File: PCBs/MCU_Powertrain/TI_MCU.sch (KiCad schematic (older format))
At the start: 1 part

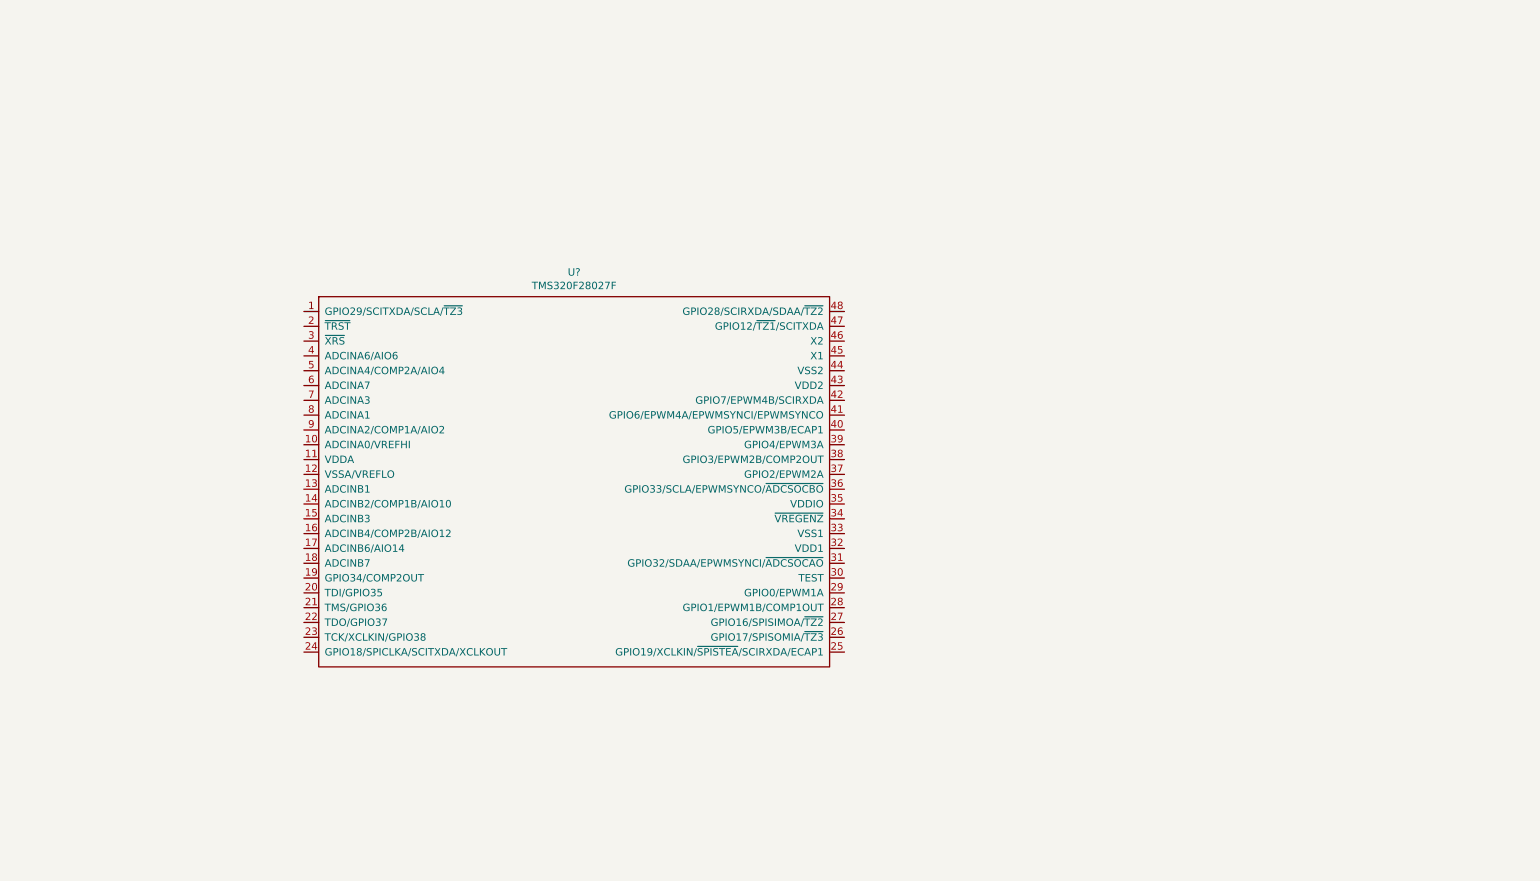
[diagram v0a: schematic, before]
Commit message: Updated TI_MCU Sheet
-Added all required components onto the TI-MCU sheet other than the external connections (header pins on the dev board)
- Added pulldown and pullup resistors for proper JTAG debug and flashing functionality.
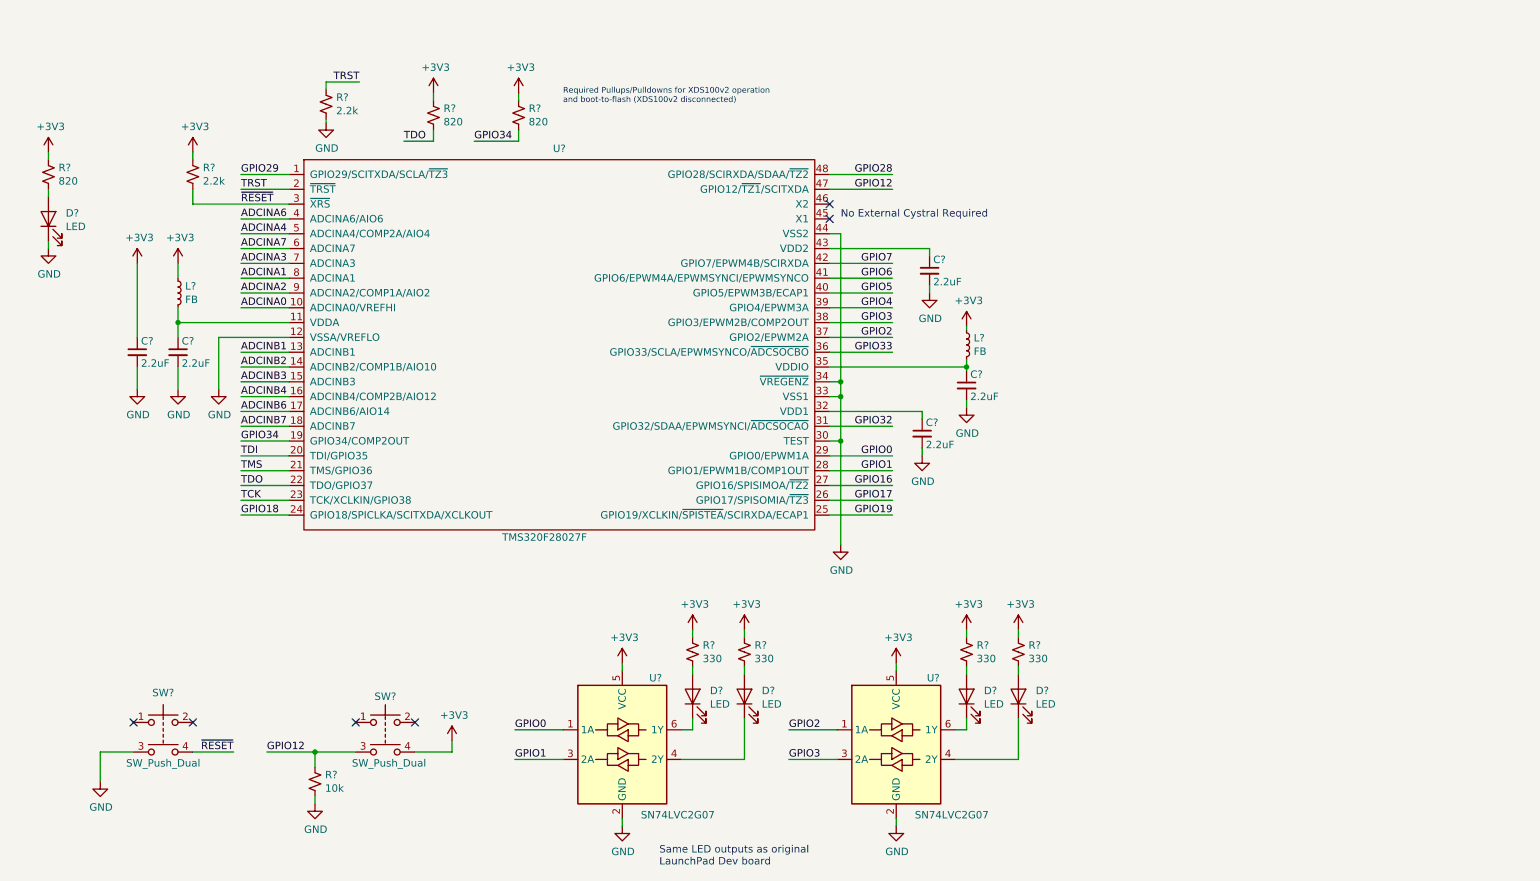
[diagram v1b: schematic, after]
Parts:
- added C? (x5): 2.2uF, symbol Device:C_Small
- added D? (x5): LED, symbol Device:LED
- added L? (x2): FB, symbol Device:L_Small
- added R? (x3): 820, symbol Device:R_Small_US
- added R? (x2): 2.2k, symbol Device:R_Small_US
- added R? (x4): 330, symbol Device:R_Small_US
- added R?: 10k, symbol Device:R_Small_US
- added SW? (x2): SW_Push_Dual, symbol Switch:SW_Push_Dual
- added U? (x2): SN74LVC2G07, Package_SO:VSSOP-8_2.4x2.1mm_P0.5mm, symbol MCU_Powertrain:SN74LVC2G07
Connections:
- net GPIO29: now reaches U?.1 (GPIO29/SCITXDA/SCLA/~TZ3~)
- net ADCINA0: now reaches U?.10 (ADCINA0/VREFHI)
- net at U?.11 (VDDA): now also C?.1, L?.2
- net GND: now reaches U?.12 (VSSA/VREFLO)
- net GND: now also U?.30 (TEST), U?.33 (VSS1), U?.34 (~VREGENZ~), U?.44 (VSS2), C?.2, C?.2, C?.2, C?.2, C?.2, D?.1 (K), R?.2, R?.2, SW?.3, U?.2 (GND), U?.2 (GND)
- net ADCINB1: now reaches U?.13 (ADCINB1)
- net ADCINB2: now reaches U?.14 (ADCINB2/COMP1B/AIO10)
- net ADCINB3: now reaches U?.15 (ADCINB3)
- net ADCINB4: now reaches U?.16 (ADCINB4/COMP2B/AIO12)
- net ADCINB6: now reaches U?.17 (ADCINB6/AIO14)
- net ADCINB7: now reaches U?.18 (ADCINB7)
- net GPIO34: now reaches U?.19 (GPIO34/COMP2OUT)
- net GPIO34: now also R?.2
- net TRST: now reaches U?.2 (~TRST~)
- net TRST: now also R?.1
- net TDI: now reaches U?.20 (TDI/GPIO35)
- net TMS: now reaches U?.21 (TMS/GPIO36)
- net TDO: now reaches U?.22 (TDO/GPIO37)
- net TDO: now also R?.2
- net TCK: now reaches U?.23 (TCK/XCLKIN/GPIO38)
- net GPIO18: now reaches U?.24 (GPIO18/SPICLKA/SCITXDA/XCLKOUT)
- net GPIO19: now reaches U?.25 (GPIO19/XCLKIN/~SPISTEA~/SCIRXDA/ECAP1)
- net GPIO17: now reaches U?.26 (GPIO17/SPISOMIA/~TZ3)
- net GPIO16: now reaches U?.27 (GPIO16/SPISIMOA/~TZ2~)
- net GPIO1: now reaches U?.28 (GPIO1/EPWM1B/COMP1OUT)
- net GPIO1: now also U?.3 (2A)
- net GPIO0: now reaches U?.29 (GPIO0/EPWM1A)
- net GPIO0: now also U?.1 (1A)
- net ~RESET~: now reaches U?.3 (~XRS~)
- net ~RESET~: now also R?.2, SW?.4
- net GPIO32: now reaches U?.31 (GPIO32/SDAA/EPWMSYNCI/~ADCSOCAO~)
- net at U?.32 (VDD1): now also C?.1
- net at U?.35 (VDDIO): now also C?.1, L?.2
- net GPIO33: now reaches U?.36 (GPIO33/SCLA/EPWMSYNCO/~ADCSOCBO~)
- net GPIO2: now reaches U?.37 (GPIO2/EPWM2A)
- net GPIO2: now also U?.1 (1A)
- net GPIO3: now reaches U?.38 (GPIO3/EPWM2B/COMP2OUT)
- net GPIO3: now also U?.3 (2A)
- net GPIO4: now reaches U?.39 (GPIO4/EPWM3A)
- net ADCINA6: now reaches U?.4 (ADCINA6/AIO6)
- net GPIO5: now reaches U?.40 (GPIO5/EPWM3B/ECAP1)
- net GPIO6: now reaches U?.41 (GPIO6/EPWM4A/EPWMSYNCI/EPWMSYNCO)
- net GPIO7: now reaches U?.42 (GPIO7/EPWM4B/SCIRXDA)
- net at U?.43 (VDD2): now also C?.1
- net GPIO12: now reaches U?.47 (GPIO12/~TZ1~/SCITXDA)
- net GPIO12: now also R?.1, SW?.3
- net GPIO28: now reaches U?.48 (GPIO28/SCIRXDA/SDAA/~TZ2~)
- net ADCINA4: now reaches U?.5 (ADCINA4/COMP2A/AIO4)
- net ADCINA7: now reaches U?.6 (ADCINA7)
- net ADCINA3: now reaches U?.7 (ADCINA3)
- net ADCINA1: now reaches U?.8 (ADCINA1)
- net ADCINA2: now reaches U?.9 (ADCINA2/COMP1A/AIO2)
- new net: D?.2 (A), R?.2 (x5)
- new net: D?.1 (K), U?.4 (2Y) (x2)
- new net: D?.1 (K), U?.6 (1Y) (x2)
- new net +3V3: C?.1, L?.1, L?.1, R?.1, R?.1, R?.1, R?.1, R?.1, R?.1, R?.1, R?.1, SW?.4, U?.5 (VCC), U?.5 (VCC)
- no-connect marks 0 -> 6
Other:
- note added: "No External Cystral Required"
- note added: "Required Pullups/Pulldowns for XDS100v2 operation \nand boot-to-flash (XDS100v2 disconnected)"
- note added: "Same LED outputs as original\nLaunchPad Dev board"
- moved on the sheet: U?

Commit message: More Schematic Changes
- Connected TI_MCU schematic to Powertrain schematic
- Added power input
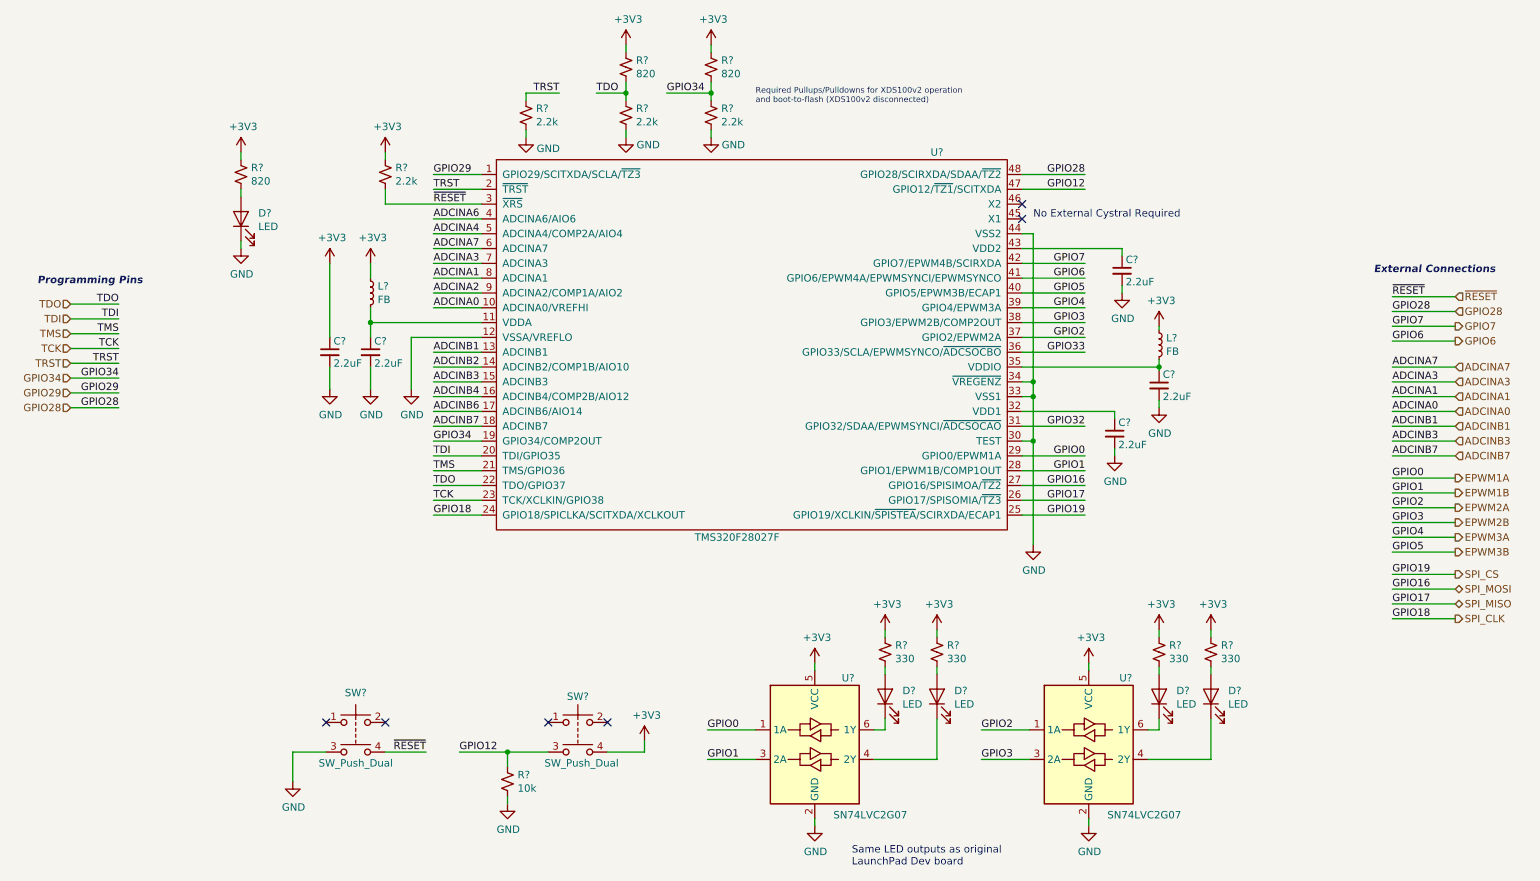
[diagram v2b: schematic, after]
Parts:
- added R? (x2): 2.2k, symbol Device:R_Small_US
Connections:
- net GND: now also R?.2, R?.2
- net GPIO34: now also R?.1
- net TDO: now also R?.1
- net GPIO0 renamed EPWM1A
- net GPIO1 renamed EPWM1B
- net GPIO16 renamed SPI_MOSI
- net GPIO17 renamed SPI_MISO
- net GPIO18 renamed SPI_CLK
- net GPIO19 renamed SPI_CS
- net GPIO2 renamed EPWM2A
- net GPIO3 renamed EPWM2B
- net GPIO4 renamed EPWM3A
- net GPIO5 renamed EPWM3B
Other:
- note added: "External Connections"
- note added: "Programming Pins"
- moved on the sheet: C?, D?, L?, R?, SW?, U?

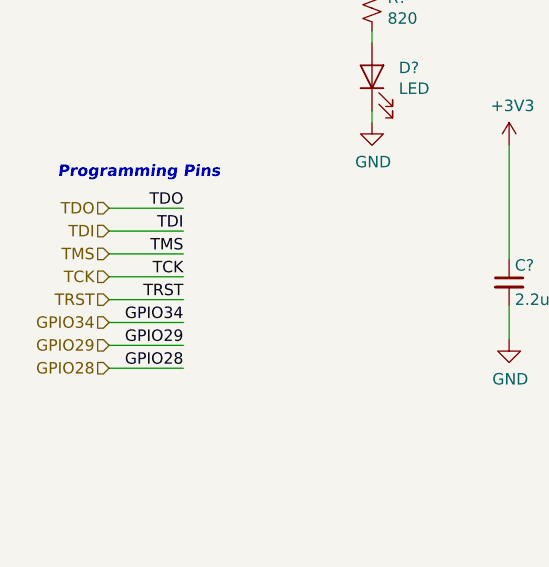
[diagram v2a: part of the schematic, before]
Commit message: Added Programming Headers
- Inserted programming headers based on latest header format from custom XDS100v2 programmer.
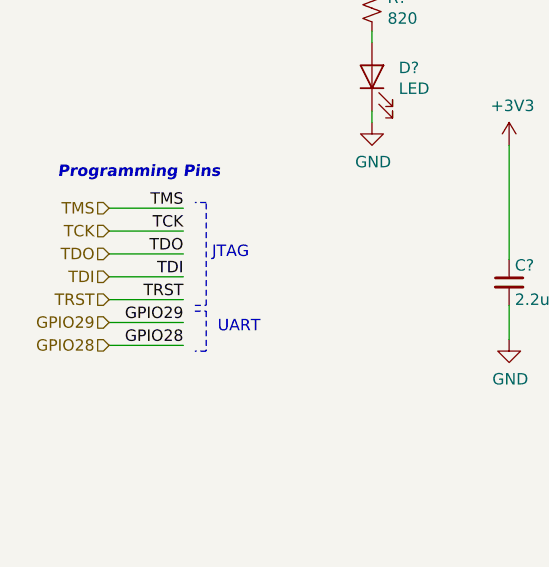
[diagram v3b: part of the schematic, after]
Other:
- note added: "JTAG"
- note added: "UART"
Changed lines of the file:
@@
 Wire Wire Line
 	5275 1325 5275 1375
+Text HLabel 950  3000 0    50   Input ~ 0
+GPIO29
 Text HLabel 950  3100 0    50   Input ~ 0
-GPIO29
-Text HLabel 950  3200 0    50   Input ~ 0
 GPIO28
-Text HLabel 950  3000 0    50   Input ~ 0
-GPIO34
 Text HLabel 950  2900 0    50   Input ~ 0
 TRST
+Text HLabel 950  2600 0    50   Input ~ 0
+TCK
+Text HLabel 950  2500 0    50   Input ~ 0
+TMS
 Text HLabel 950  2800 0    50   Input ~ 0
-TCK
+TDI
 Text HLabel 950  2700 0    50   Input ~ 0
-TMS
-Text HLabel 950  2600 0    50   Input ~ 0
-TDI
-Text HLabel 950  2500 0    50   Input ~ 0
 TDO
+Wire Wire Line
+	950  2700 1275 2700
+Wire Wire Line
+	950  2800 1275 2800
 Wire Wire Line
 	950  2500 1275 2500
 Wire Wire Line
 	950  2600 1275 2600
-Wire Wire Line
-	950  2700 1275 2700
-Wire Wire Line
-	950  2800 1275 2800
 Wire Wire Line
 	950  2900 1275 2900
@@
 Wire Wire Line
 	950  3100 1275 3100
-Wire Wire Line
-	950  3200 1275 3200
+Text Label 1275 2800 2    50   ~ 0
+TDI
+Text Label 1275 2500 2    50   ~ 0
+TMS
+Text Label 1275 2700 2    50   ~ 0
+TDO
 Text Label 1275 2600 2    50   ~ 0
-TDI
-Text Label 1275 2700 2    50   ~ 0
-TMS
-Text Label 1275 2500 2    50   ~ 0
-TDO
-Text Label 1275 2800 2    50   ~ 0
 TCK
 Text Label 1275 2900 2    50   ~ 0
 TRST
 Text Label 1275 3000 2    50   ~ 0
-GPIO34
+GPIO29
 Text Label 1275 3100 2    50   ~ 0
-GPIO29
-Text Label 1275 3200 2    50   ~ 0
 GPIO28
+Wire Notes Line
+	1325 2950 1375 2950
+Wire Notes Line
+	1375 2950 1375 3125
+Wire Notes Line
+	1375 3125 1325 3125
+Wire Notes Line
+	1325 2925 1375 2925
+Wire Notes Line
+	1375 2925 1375 2475
+Wire Notes Line
+	1375 2475 1325 2475
+Text Notes 1400 2725 0    50   ~ 0
+JTAG
+Text Notes 1425 3050 0    50   ~ 0
+UART
 $EndSCHEMATC

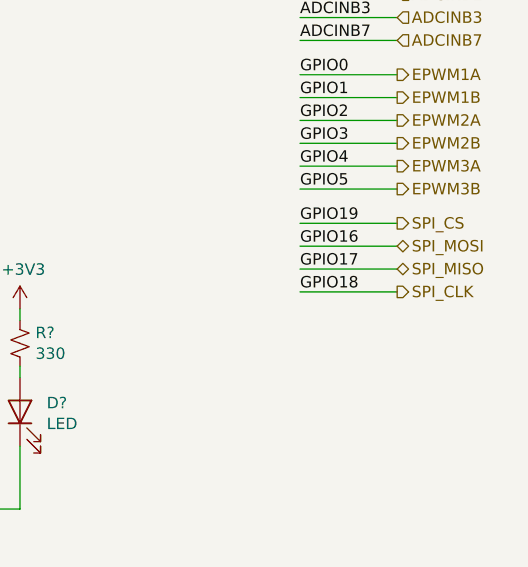
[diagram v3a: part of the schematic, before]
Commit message: CAN and Minor Changes
- Added CAN Controller (MCP2515) and CAN transciever
- Added net-ties to shunts
- Removed all +12V references and replaced with +BATT references.
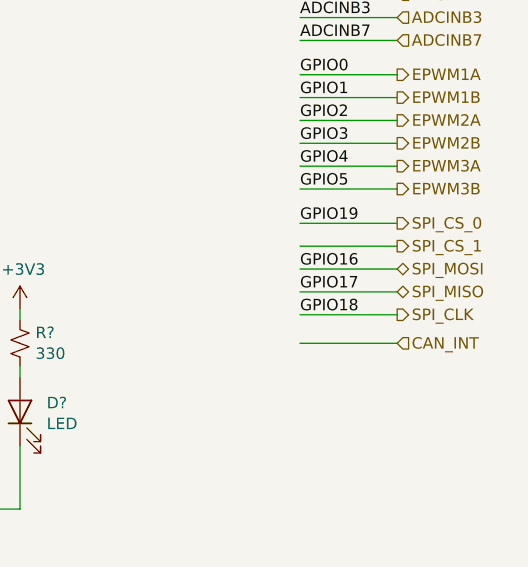
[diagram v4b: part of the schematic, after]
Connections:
- net SPI_CS renamed SPI_CS_0
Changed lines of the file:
@@
 Text HLabel 10300 2550 2    50   Input ~ 0
 GPIO28
-Text HLabel 10300 4625 2    50   Output ~ 0
+Text HLabel 10300 4725 2    50   Output ~ 0
 SPI_CLK
 Text HLabel 10300 2925 2    50   Input ~ 0
@@
 EPWM3B
 Text HLabel 10300 4325 2    50   Output ~ 0
-SPI_CS
+SPI_CS_0
 Text HLabel 10300 2450 2    50   Input ~ 0
 ~RESET~
-Text HLabel 10300 4425 2    50   BiDi ~ 0
+Text HLabel 10300 4525 2    50   BiDi ~ 0
 SPI_MOSI
-Text HLabel 10300 4525 2    50   BiDi ~ 0
+Text HLabel 10300 4625 2    50   BiDi ~ 0
 SPI_MISO
 Text HLabel 10300 2750 2    50   Output ~ 0
@@
 	10300 4325 9875 4325
 Wire Wire Line
-	10300 4425 9875 4425
-Wire Wire Line
 	10300 4525 9875 4525
 Wire Wire Line
 	10300 4625 9875 4625
+Wire Wire Line
+	10300 4725 9875 4725
 Wire Wire Line
 	10300 2450 9875 2450
@@
 Text Label 9875 2550 0    50   ~ 0
 GPIO28
-Text Label 9875 4625 0    50   ~ 0
+Text Label 9875 4725 0    50   ~ 0
 GPIO18
 Text Label 9875 3675 0    50   ~ 0
@@
 Text Label 9875 4325 0    50   ~ 0
 GPIO19
-Text Label 9875 4425 0    50   ~ 0
+Text Label 9875 4525 0    50   ~ 0
 GPIO16
-Text Label 9875 4525 0    50   ~ 0
+Text Label 9875 4625 0    50   ~ 0
 GPIO17
 Text Label 9875 2650 0    50   ~ 0
@@
 Text Notes 1425 3050 0    50   ~ 0
 UART
+Text HLabel 10300 4425 2    50   Output ~ 0
+SPI_CS_1
+Wire Wire Line
+	10300 4425 9875 4425
+Text HLabel 10300 4850 2    50   Input ~ 0
+CAN_INT
+Wire Wire Line
+	10300 4850 9875 4850
 $EndSCHEMATC
